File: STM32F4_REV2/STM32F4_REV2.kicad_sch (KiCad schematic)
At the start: 35 parts, among them Q1 AO3401A, SW1 SW_SPDT, U1 STM32F405RGT6, Y1 16MHz

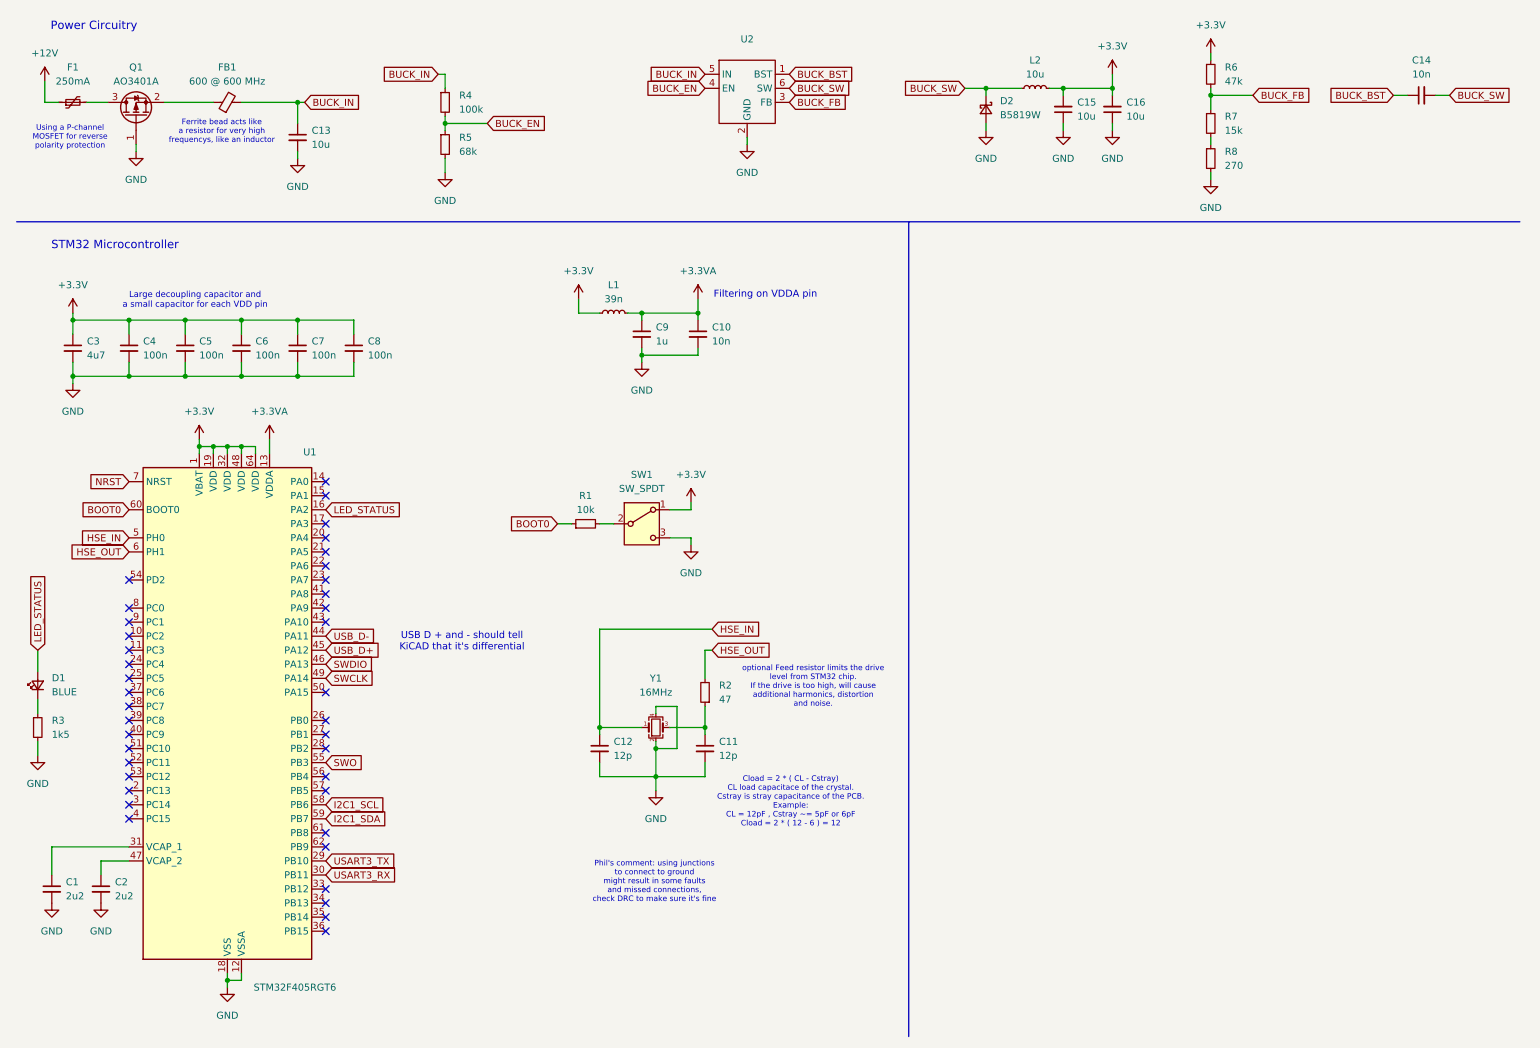
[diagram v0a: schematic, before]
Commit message: Finished Footprints
Finished selecting footprints.
Used Phi'ls selections but for USB Micro B I found in my own.
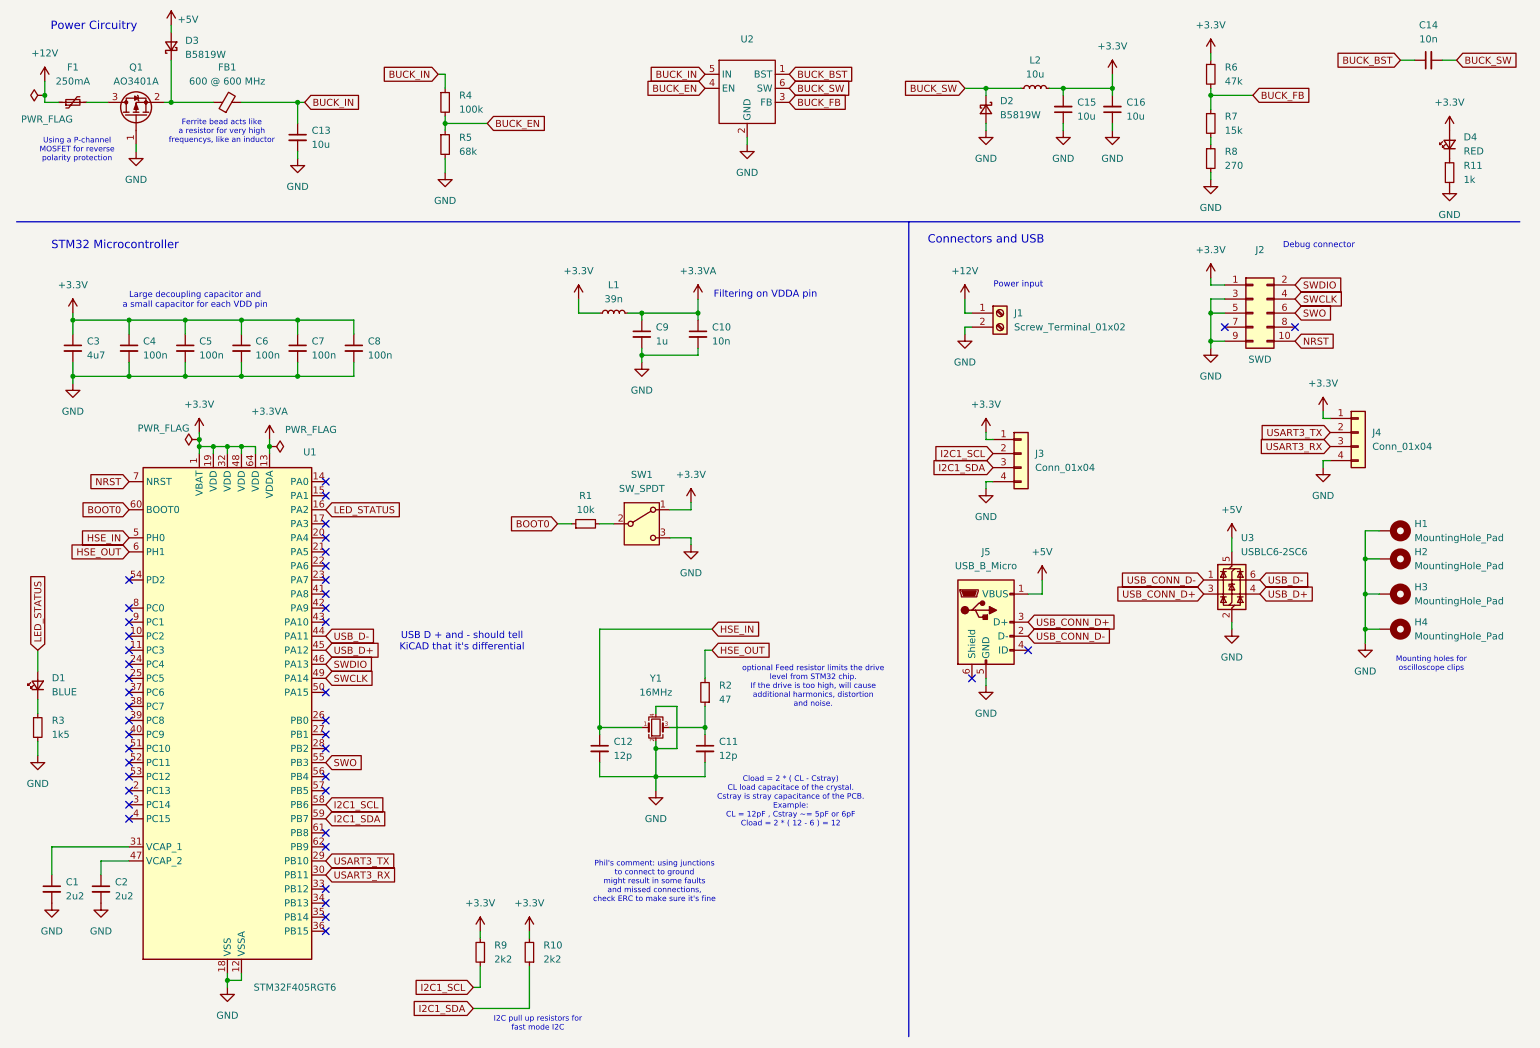
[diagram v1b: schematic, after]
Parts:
- added D3: B5819W, Diode_SMD:D_SOD-123, symbol Device:D_Schottky_Small
- added D4: RED, LED_SMD:LED_0603_1608Metric, symbol Device:LED_Small
- added H1, H2, H3, H4: MountingHole_Pad, MountingHole:MountingHole_4.3mm_M4_Pad_Via, symbol Mechanical:MountingHole_Pad
- added J1: Screw_Terminal_01x02, TerminalBlock_Phoenix:TerminalBlock_Phoenix_PT-1,5-2-3.5-H_1x02_P3.50mm_Horizontal, symbol Connector:Screw_Terminal_01x02
- added J2: SWD, Connector_PinSocket_1.27mm:PinSocket_2x05_P1.27mm_Vertical_SMD, symbol Connector_Generic:Conn_02x05_Odd_Even
- added J3, J4: Conn_01x04, Connector_Molex:Molex_PicoBlade_53048-0410_1x04_P1.25mm_Horizontal, symbol Connector_Generic:Conn_01x04
- added J5: USB_B_Micro, Connector_USB:USB_Micro-B_Amphenol_10118194_Horizontal, symbol Connector:USB_B_Micro
- added R10, R9: 2k2, Resistor_SMD:R_0402_1005Metric, symbol Device:R_Small
- added R11: 1k, Resistor_SMD:R_0603_1608Metric, symbol Device:R_Small
- added U3: USBLC6-2SC6, Package_TO_SOT_SMD:SOT-23-6, symbol Power_Protection:USBLC6-2SC6
- C1, C10, C14, C2, C3: footprint (none) -> Capacitor_SMD:C_0603_1608Metric
- C11, C12, C4, C5, C6, C7, C8, C9: footprint (none) -> Capacitor_SMD:C_0402_1005Metric
- C13, C15, C16: footprint (none) -> Capacitor_SMD:C_1206_3216Metric
- D1: footprint (none) -> LED_SMD:LED_0603_1608Metric
- D2: footprint (none) -> Diode_SMD:D_SOD-123
- F1: footprint (none) -> Fuse:Fuse_1206_3216Metric
- FB1: footprint (none) -> Inductor_SMD:L_0805_2012Metric
- L1: footprint (none) -> Inductor_SMD:L_0402_1005Metric
- L2: footprint (none) -> Inductor_SMD:L_Sunlord_MWSA0503S
- R1, R2: footprint (none) -> Resistor_SMD:R_0402_1005Metric
- R3, R4, R5, R6, R7, R8: footprint (none) -> Resistor_SMD:R_0603_1608Metric
- SW1: footprint (none) -> Button_Switch_SMD:SW_SPDT_PCM12
- U2: footprint (none) -> Package_TO_SOT_SMD:SOT-23-6
- Y1: footprint (none) -> Crystal:Crystal_SMD_3225-4Pin_3.2x2.5mm
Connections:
- net +12V: now also J1.1 (Pin_1)
- net +3.3V: now also D4.2 (A), J2.1 (Pin_1), J3.1 (Pin_1), J4.1 (Pin_1), R10.2, R9.2
- net GND: now also H1.1, H2.1, H3.1, H4.1, J1.2 (Pin_2), J2.3 (Pin_3), J2.5 (Pin_5), J2.9 (Pin_9), J3.4 (Pin_4), J4.4 (Pin_4), J5.5 (GND), R11.2, U3.2 (GND)
- net I2C1_SCL: now also J3.2 (Pin_2), R9.1
- net I2C1_SDA: now also J3.3 (Pin_3), R10.1
- net NRST: now also J2.10 (Pin_10)
- net SWCLK: now also J2.4 (Pin_4)
- net SWDIO: now also J2.2 (Pin_2)
- net SWO: now also J2.6 (Pin_6)
- net USART3_RX: now also J4.3 (Pin_3)
- net USART3_TX: now also J4.2 (Pin_2)
- net USB_D+: now also U3.4 (I/O2)
- net USB_D-: now also U3.6 (I/O1)
- net at FB1.1, Q1.2 (S): now also D3.1 (K)
- new net: D4.1 (K), R11.1
- new net +5V: D3.2 (A), J5.1 (VBUS), U3.5 (VBUS)
- new net USB_CONN_D+: J5.3 (D+), U3.3 (I/O2)
- new net USB_CONN_D-: J5.2 (D-), U3.1 (I/O1)
- no-connect marks 39 -> 43
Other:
- note added: "Connectors and USB"
- note added: "Debug connector"
- note added: "I2C pull up resistors for fast mode I2C"
- note added: "Mounting holes for oscilloscope clips"
- note added: "Phil's comment: using junctions to connect to ground might result in some faults and missed connections, check ERC to make sure it's fine"
- note added: "Power input"
- note removed: "Phil's comment: using junctions to connect to ground might result in some faults and missed connections, check DRC to make sure it's fine"
- moved on the sheet: C14

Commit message: Layout finished
Finished the layout, need to route
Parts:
- C10: footprint Capacitor_SMD:C_0603_1608Metric -> Capacitor_SMD:C_0402_1005Metric
- J5: footprint Connector_USB:USB_Micro-B_Amphenol_10118194_Horizontal -> Connector_USB:USB_Micro-B_Amphenol_10118193-0001LF_Horizontal
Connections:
- net +12V: now also Q1.3 (D); no longer F1.1
- net at D3.1 (K), Q1.2 (S): now also F1.1; no longer FB1.1
- net at F1.2: now also FB1.1; no longer Q1.3 (D)
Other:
- moved on the sheet: C13, F1, FB1, R4, R5
